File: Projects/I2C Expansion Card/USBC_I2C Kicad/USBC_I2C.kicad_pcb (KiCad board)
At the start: 2 copper layers, 26 x 30 mm, 23 parts, among them U1 MCP2221A

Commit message: Fixing some DRC
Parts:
- removed the REF** at (89.8, 69.3)
- removed TP1, TP2 (x2): TestPoint, TestPoint:TestPoint_Pad_1.5x1.5mm
- added ?: , , B.Cu at (102.8, 58.4)
- added ?: , , B.Cu at (90.9, 58.4)
- added SW1: SW_DIP_x04, Button_Switch_SMD:SW_DIP_SPSTx04_Slide_Copal_CHS-04B_W7.62mm_P1.27mm, F.Cu at (89.8, 69.3)
- added TP3: TestPoint, TestPoint:TestPoint_Pad_1.5x1.5mm, F.Cu at (90.9, 58.4)
- U1: value MCP2221A -> MCP2221AxSL
- moved TP3 0.32 mm to (102.8, 58.4)
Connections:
- net SCL renamed Net-(U1-SCL)
- net SDA renamed Net-(U1-SDA)
- REF** pad 2: (no net) -> Out0 (x4)
- REF** pad 3: (no net) -> Out1 (x3)
- REF** pad 2: (no net) -> Out1
- U1 pad 5: unconnected-(U1-URx-Pad5) -> Net-(U1-URx)
- U1 pad 6: unconnected-(U1-UTx-Pad6) -> Net-(U1-UTx)
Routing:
- net (no net): track 67.5 -> 0.00 mm
- net Out0: track 0.00 -> 35.2 mm
- net Out1: track 0.00 -> 32.2 mm
- net unconnected-(U1-UTx-Pad6): track 18.7 -> 0.00 mm
- net Net-(U1-UTx): track 0.00 -> 18.7 mm
- net unconnected-(U1-URx-Pad5): track 16.1 -> 0.00 mm
- net Net-(U1-URx): track 0.00 -> 16.1 mm

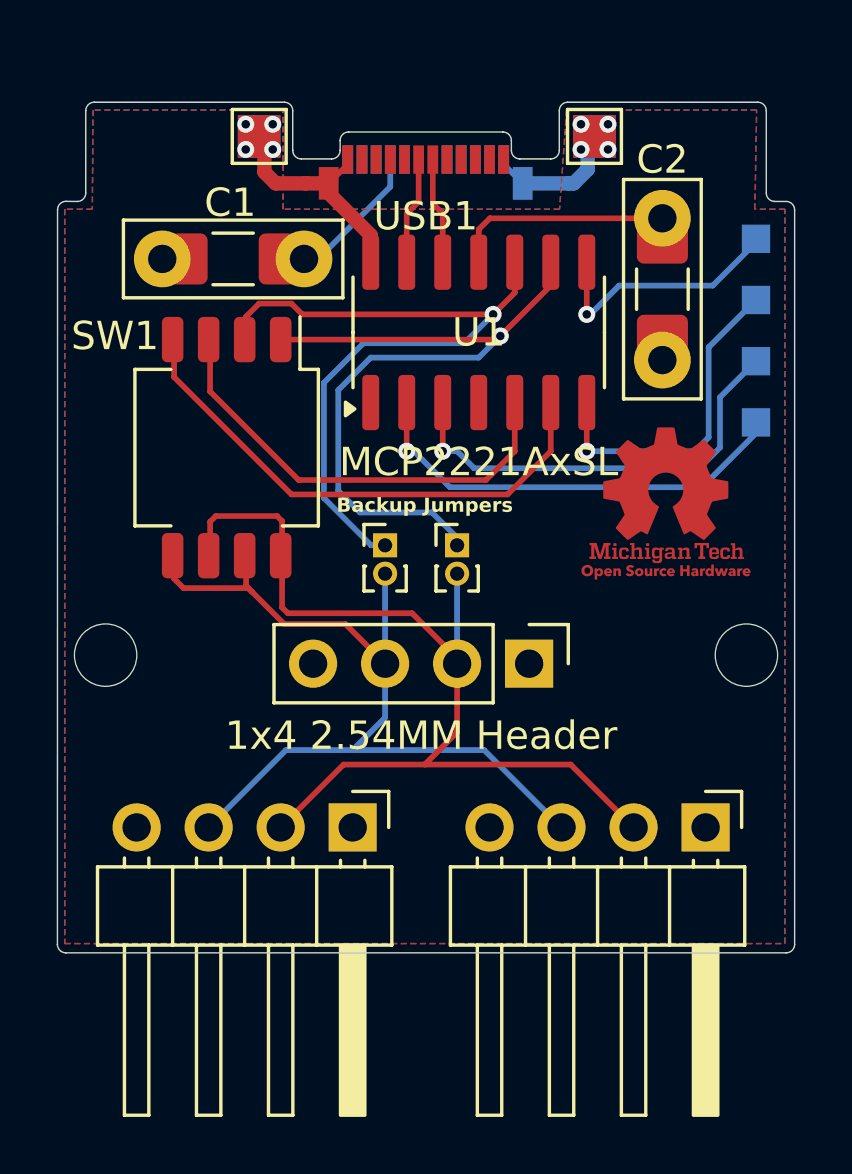
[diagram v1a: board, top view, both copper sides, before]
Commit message: Added USB PD Resistors
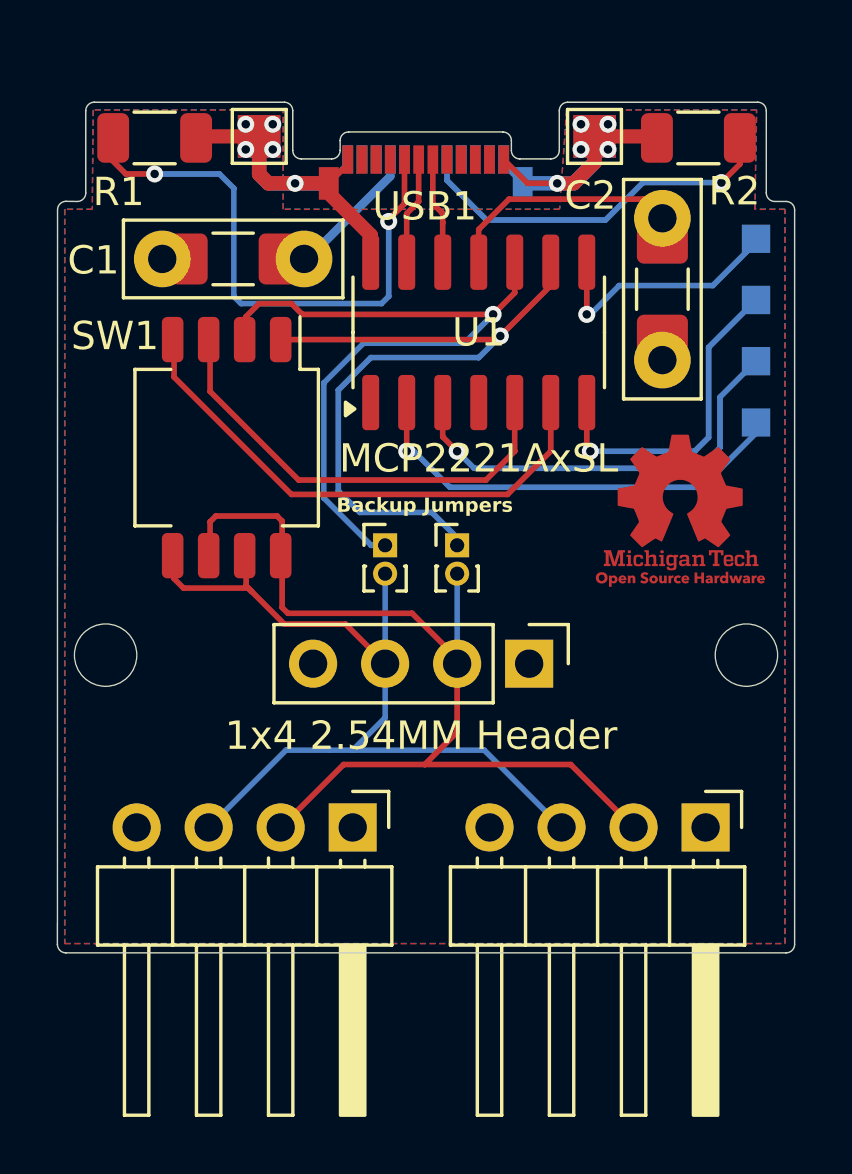
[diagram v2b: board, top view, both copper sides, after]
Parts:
- added R1: 5.1k, Resistor_SMD:R_1206_3216Metric, F.Cu at (87.2, 58.4)
- added R2: Resistors TBD, Resistor_SMD:R_1206_3216Metric, F.Cu at (106.4, 58.4)
- moved G*** 0.57 mm to (105.8, 71.6)
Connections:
- USB1 pad A5: unconnected-(USB1-CC-PadA5) -> Net-(USB1-CC)
- USB1 pad B5: unconnected-(USB1-VCONN-PadB5) -> Net-(USB1-VCONN)
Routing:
- net Net-(USB1-CC): track 0.00 -> 20.7 mm, vias 0 -> 2
- net GND: track 14.6 -> 28.7 mm, vias 8 -> 10
- net Net-(USB1-VCONN): track 0.00 -> 13.4 mm, vias 0 -> 1
- net Net-(U1-VUSB): track 10.0 -> 10.6 mm

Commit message: Added OCP
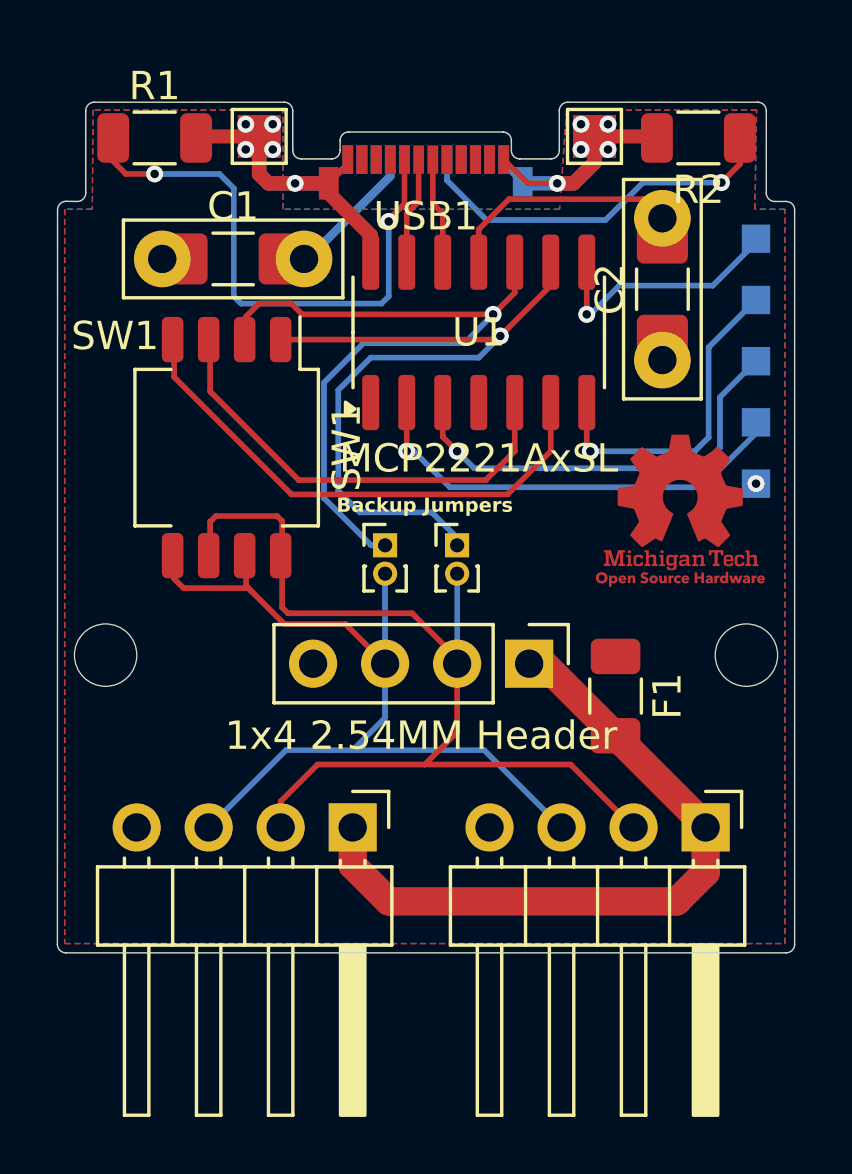
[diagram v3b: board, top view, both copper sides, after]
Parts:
- added F1: Polyfuse, Fuse:Fuse_1206_3216Metric, F.Cu at (103.5, 78.1)
- added REF**: TestPoint_Pad_1.0x1.0mm, TestPoint:TestPoint_Pad_1.0x1.0mm, B.Cu at (108.5, 70.6)
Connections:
- C1 pad 2: 5V -> Net-(U1-VDD)
- REF** pad 1: 5V -> Vo (x3)
- REF** pad 1: 5V -> Net-(U1-VDD)
- U1 pad 1: 5V -> Net-(U1-VDD)
- USB1 pad A4: 5V -> Net-(U1-VDD)
- USB1 pad A9: 5V -> Net-(U1-VDD)
- USB1 pad B4: 5V -> Net-(U1-VDD)
- USB1 pad B9: 5V -> Net-(U1-VDD)
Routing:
- net Vo: track 0.00 -> 25.6 mm
- net 5V: track 6.73 -> 0.00 mm
- net Net-(U1-VDD): track 0.00 -> 6.60 mm, vias 0 -> 1
- net Out0: track 35.2 -> 35.8 mm
- added copper zone on F.Cu, net Net-(U1-VDD)
- removed copper zone on F.Cu, net 5V

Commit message: Reworked the PCB to better route traces
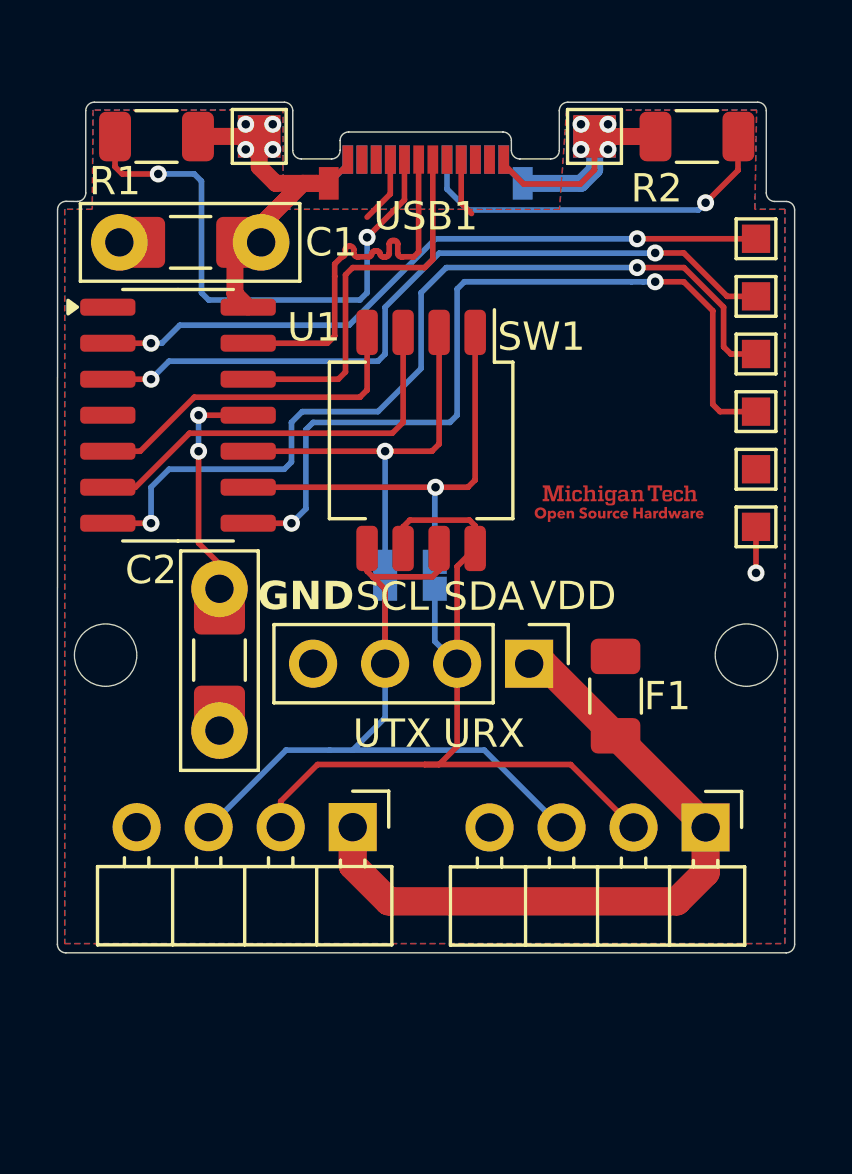
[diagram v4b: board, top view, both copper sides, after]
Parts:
- removed the REF** at (108.5, 68.5)
- removed the REF** at (108.5, 66.3)
- removed the REF** at (108.5, 64.1)
- removed the REF** at (92.5, 62.7)
- removed the REF** at (95.4, 72.8)
- removed the REF** at (97.9, 72.8)
- removed the REF** at (105.2, 61.3)
- removed the REF** at (108.5, 70.6)
- added 2x Pads: Jumper Pads, Custom Parts:Jumper Pads, B.Cu at (97.1, 73.3)
- added 2x Pads: Jumper Pads, Custom Parts:Jumper Pads, B.Cu at (95.4, 73.3)
- added REF**: TestPoint_Pad_1.0x1.0mm, TestPoint:TestPoint_Pad_1.0x1.0mm, F.Cu at (108.5, 66.0)
- added REF**: TestPoint_Pad_1.0x1.0mm, TestPoint:TestPoint_Pad_1.0x1.0mm, F.Cu at (108.5, 64.0)
- added REF**: TestPoint_Pad_1.0x1.0mm, TestPoint:TestPoint_Pad_1.0x1.0mm, F.Cu at (108.5, 70.1)
- added REF**: TestPoint_Pad_1.0x1.0mm, TestPoint:TestPoint_Pad_1.0x1.0mm, F.Cu at (108.5, 72.1)
- added REF**: TestPoint_Pad_1.0x1.0mm, TestPoint:TestPoint_Pad_1.0x1.0mm, F.Cu at (108.5, 68.1)
- REF**: moved to F.Cu
- moved C2 20.4 mm to (89.5, 76.8)
- moved U1 11.0 mm to (88.1, 68.2), turned to 0 degrees
- moved SW1 6.86 mm to (96.6, 69.1)
- moved G*** 3.14 mm to (103.6, 69.3)
- moved C1 1.61 mm to (88.5, 62.1), turned to 180 degrees
- moved R1 0.08 mm to (87.3, 58.4)
- moved R2 0.07 mm to (106.4, 58.4)
- turned REF** to 0 degrees
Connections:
- SW1 pad 3: Net-(U1-URx) -> Net-(U1-UTx)
- SW1 pad 4: Net-(U1-UTx) -> Net-(U1-URx)
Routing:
- net Net-(D4-A): track 8.86 -> 29.5 mm, vias 1 -> 2
- net Net-(D3-A): track 11.7 -> 31.8 mm, vias 1 -> 2
- net Net-(U1-SCL): track 25.9 -> 14.7 mm
- net Net-(D2-A): track 15.4 -> 26.3 mm, vias 1 -> 2
- net Net-(U1-SDA): track 26.4 -> 16.0 mm
- net Net-(U1-D-): track 3.77 -> 13.8 mm
- net Net-(U1-D+): track 3.80 -> 13.7 mm
- net Net-(D1-A): track 16.0 -> 24.4 mm, vias 1 -> 2
- net GND: track 28.7 -> 34.7 mm, vias 10 -> 9
- net Out0: track 35.8 -> 30.9 mm
- net Net-(U1-UTx): track 18.7 -> 14.5 mm
- net Net-(U1-URx): track 16.1 -> 12.1 mm
- net Net-(U1-VUSB): track 10.6 -> 7.30 mm, vias 0 -> 2
- net Out1: track 32.2 -> 29.0 mm
- net Net-(U1-VDD): track 6.60 -> 4.43 mm, vias 1 -> 0
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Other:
- board text added: "GND"
- board text added: "SCL UTX"
- board text added: "SDA URX"
- board text added: "Switch Override"
- board text added: "VDD"
- board text removed: "1x4 2.54MM Header"
- board text removed: "Backup Jumpers"
- board text removed: "SW1"

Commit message: Swapped switches
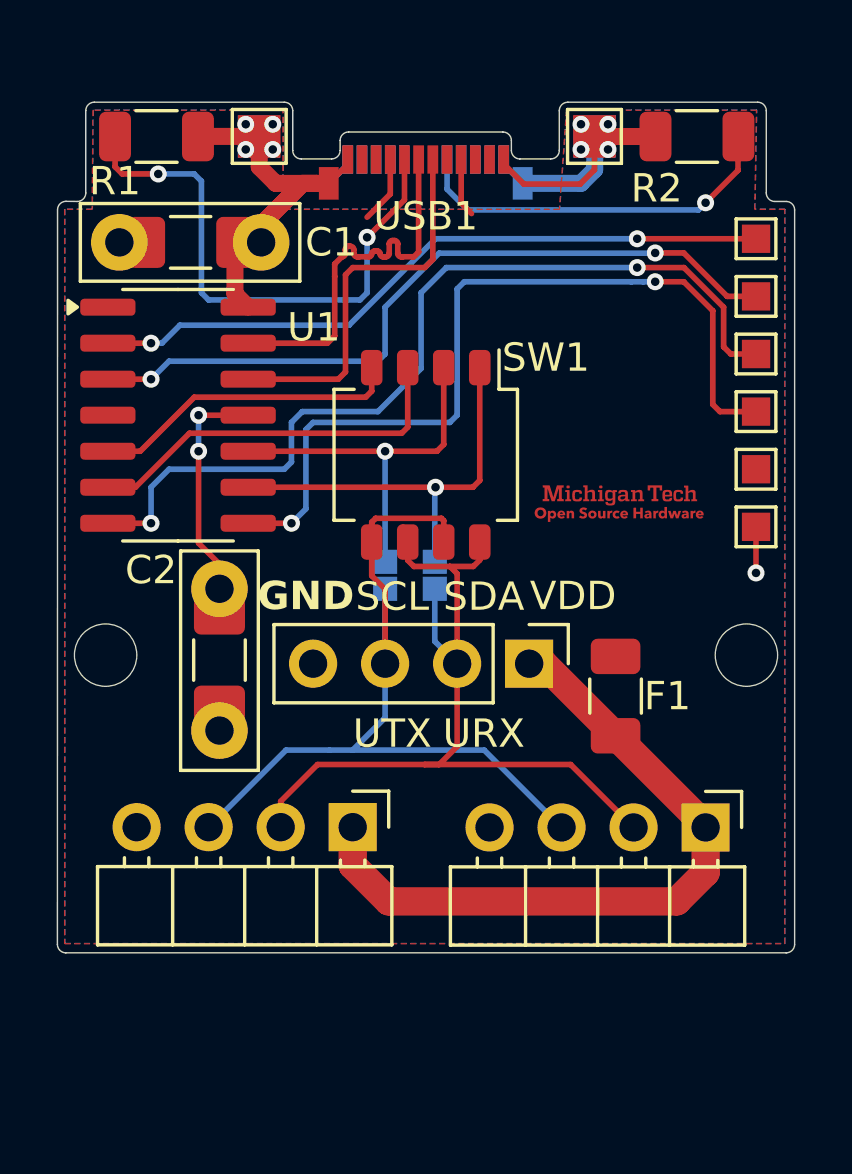
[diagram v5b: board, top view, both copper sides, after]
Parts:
- SW1: footprint Button_Switch_SMD:SW_DIP_SPSTx04_Slide_Copal_CHS-04B_W7.62mm_P1.27mm -> Button_Switch_SMD:SW_DIP_SPSTx04_Slide_Omron_A6H-4101_W6.15mm_P1.27mm
- moved SW1 0.53 mm to (96.8, 69.6)
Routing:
- net Net-(U1-SCL): track 14.7 -> 13.6 mm
- net Net-(U1-SDA): track 16.0 -> 14.9 mm
- net Out1: track 29.0 -> 30.1 mm
- net Net-(U1-UTx): track 14.5 -> 13.6 mm
- net Net-(U1-URx): track 12.1 -> 11.1 mm

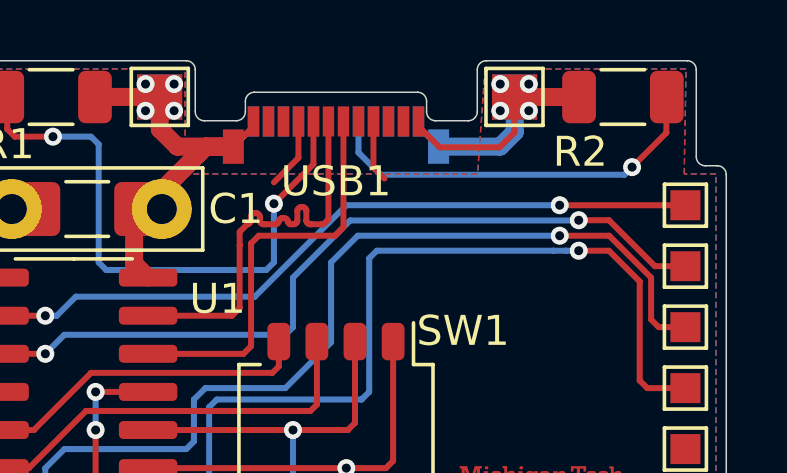
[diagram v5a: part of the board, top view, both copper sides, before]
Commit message: Rerouted a few traces
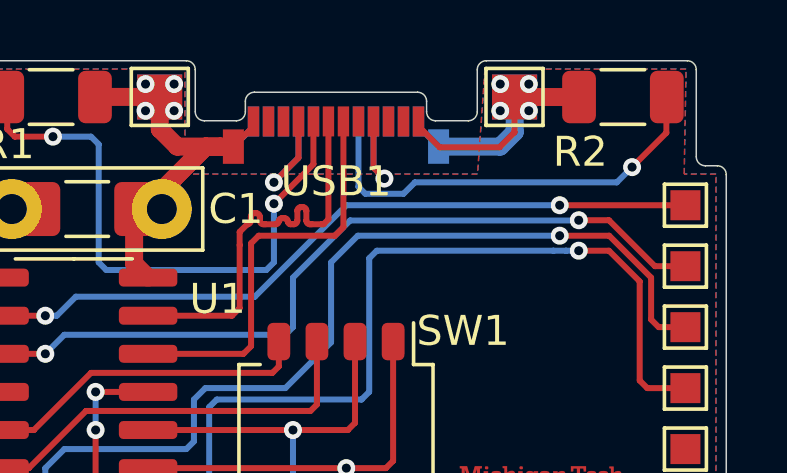
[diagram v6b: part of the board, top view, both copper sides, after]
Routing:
- net Net-(U1-VDD): track 4.43 -> 8.85 mm, vias 0 -> 2
- net Net-(USB1-VCONN): track 13.4 -> 14.6 mm
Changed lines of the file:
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@@
 		(tenting front back)
 		(pcbplotparams
-			(layerselection 0x00000000_00000000_55555555_5755fffe)
+			(layerselection 0x00000000_00000000_55555555_5755ffff)
 			(plot_on_all_layers_selection 0x00000000_00000000_00000000_00000000)
 			(disableapertmacros no)
@@
 	)
 	(segment
-		(start 106.68 60.706)
-		(end 106.426 60.96)
+		(start 97.79 61.595)
+		(end 97.56 61.365)
 		(width 0.2)
 		(layer "B.Cu")
@@
 	)
 	(segment
-		(start 106.426 60.96)
-		(end 98.298 60.96)
+		(start 106.172 61.214)
+		(end 99.441 61.214)
+		(width 0.2)
+		(layer "B.Cu")
+		(net 17)
+	)
+	(segment
+		(start 106.68 60.706)
+		(end 106.172 61.214)
 		(width 0.2)
 		(layer "B.Cu")
@@
 	)
 	(segment
-		(start 97.56 60.222)
+		(start 97.56 61.365)
 		(end 97.56 59.182)
 		(width 0.2)
@@
 	)
 	(segment
-		(start 98.298 60.96)
-		(end 97.56 60.222)
+		(start 99.06 61.595)
+		(end 97.79 61.595)
+		(width 0.2)
+		(layer "B.Cu")
+		(net 17)
+	)
+	(segment
+		(start 99.441 61.214)
+		(end 99.06 61.595)
 		(width 0.2)
 		(layer "B.Cu")
@@
 		(net 18)
 	)
+	(via
+		(at 94.742 61.214)
+		(size 0.6)
+		(drill 0.3)
+		(layers "F.Cu" "B.Cu")
+		(net 18)
+	)
+	(via
+		(at 98.425 61.087)
+		(size 0.6)
+		(drill 0.3)
+		(layers "F.Cu" "B.Cu")
+		(net 18)
+	)
+	(segment
+		(start 98.06 60.722)
+		(end 98.425 61.087)
+		(width 0.2)
+		(layer "B.Cu")
+		(net 18)
+	)
+	(segment
+		(start 94.742 61.214)
+		(end 95.56 60.396)
+		(width 0.2)
+		(layer "B.Cu")
+		(net 18)
+	)
+	(segment
+		(start 98.06 59.182)
+		(end 98.06 60.722)
+		(width 0.2)
+		(layer "B.Cu")
+		(net 18)
+	)
+	(segment
+		(start 95.56 60.396)
+		(end 95.56 59.182)
+		(width 0.2)
+		(layer "B.Cu")
+		(net 18)
+	)
